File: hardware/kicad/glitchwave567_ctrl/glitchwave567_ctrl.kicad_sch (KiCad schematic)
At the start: 22 parts, among them J1 to MAIN 2x8, SW1 Suntsu SSWFS-S01 (TAP/BYP), SW2 Suntsu SSWFS-S01 (TAP/BYP)

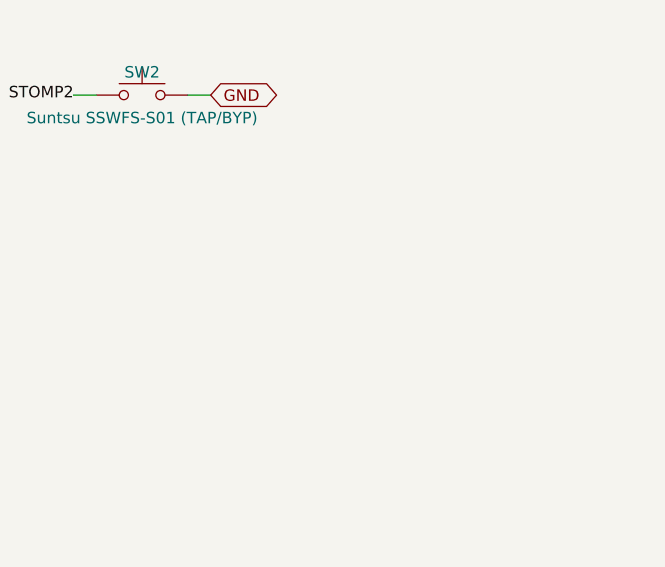
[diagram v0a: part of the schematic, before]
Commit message: hardware: root hierarchy + ERC pass on KiCad 10 (down to lib-mismatch/footprint noise + 2 intentional OTA current-sum waivers)
- root sheet ties all 8 sheets into one project (global-label connectivity, 288 comps / 259 nets stitch verified)
- fixed: U11/U12->U18/U19 ref clash, MCU cap ref clashes, env rectifier D81 feedback returned to virtual ground (was floating FW_IN2), PWR_FLAGs on PICO_VSYS + ctrl rails, off-grid buffer pin
- remaining ERC: footprint_link (assignment pending), lib_symbol_mismatch (v6 embedded vs v10 libs, cosmetic), 2x pin_to_pin Output-Output = LM13700 current summing (by design, noted on sheets)

Co-Authored-By: Claude Fable 5 <noreply@anthropic.com>
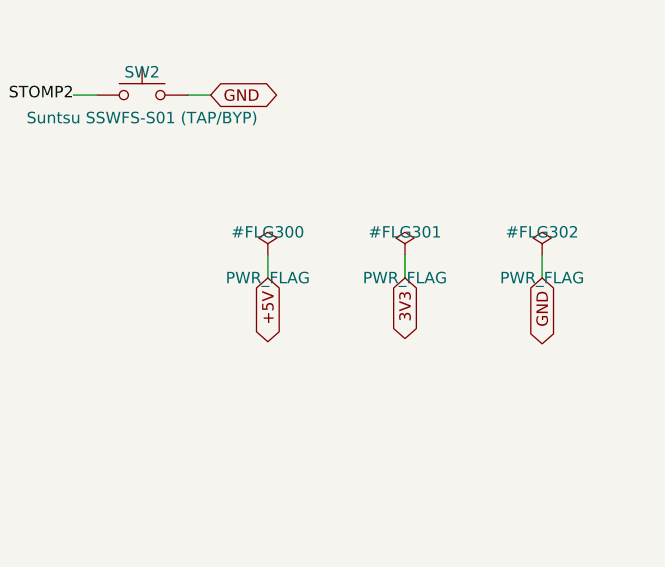
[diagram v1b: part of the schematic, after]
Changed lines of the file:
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@@
+    (stroke (width 0.0))
+  )
+  (wire (pts (xy 280.67 63.5) (xy 280.67 66.04))
+    (stroke (width 0.0))
+  )
+  (wire (pts (xy 295.91 63.5) (xy 295.91 66.04))
+    (stroke (width 0.0))
+  )
+  (wire (pts (xy 311.15 63.5) (xy 311.15 66.04))
     (stroke (width 0.0))
   )
@@
     (effects (font (size 1.27 1.27)))
   )
+  (global_label "+5V" (shape bidirectional) (at 280.67 66.04 270)
+    (effects (font (size 1.27 1.27)))
+  )
+  (global_label "3V3" (shape bidirectional) (at 295.91 66.04 270)
+    (effects (font (size 1.27 1.27)))
+  )
+  (global_label "GND" (shape bidirectional) (at 311.15 66.04 270)
+    (effects (font (size 1.27 1.27)))
+  )
   (symbol (lib_id "Connector_Generic:Conn_02x08_Odd_Even") (at 45.72 63.5 0) (unit 1)
     (in_bom yes) (on_board yes) (dnp no)
@@
         )
       )
+    )
+  )
+  (symbol (lib_id "power:PWR_FLAG") (at 280.67 63.5 0) (unit 1)
+    (in_bom yes) (on_board yes) (dnp no)
+    (property "Reference" "#FLG300" (id 0) (at 280.67 60.96 0)
+      (effects (font (size 1.27 1.27)))
+    )
+    (property "Value" "PWR_FLAG" (id 1) (at 280.67 66.04 0)
+      (effects (font (size 1.27 1.27)))
+    )
+    (property "Footprint" "" (id 2) (at 280.67 63.5 0)
+      (effects (font (size 1.27 1.27)) hide)
+    )
+    (property "Datasheet" "" (id 3) (at 280.67 63.5 0)
+      (effects (font (size 1.27 1.27)) hide)
+    )
+    (instances
+      (project "glitchwave567"
+        (path "/"
+          (reference "#FLG300") (unit 1)
+        )
+      )
+    )
+  )
+  (symbol (lib_id "power:PWR_FLAG") (at 295.91 63.5 0) (unit 1)
+    (in_bom yes) (on_board yes) (dnp no)
+    (property "Reference" "#FLG301" (id 0) (at 295.91 60.96 0)
+      (effects (font (size 1.27 1.27)))
+    )
+    (property "Value" "PWR_FLAG" (id 1) (at 295.91 66.04 0)
+      (effects (font (size 1.27 1.27)))
+    )
+    (property "Footprint" "" (id 2) (at 295.91 63.5 0)
+      (effects (font (size 1.27 1.27)) hide)
+    )
+    (property "Datasheet" "" (id 3) (at 295.91 63.5 0)
+      (effects (font (size 1.27 1.27)) hide)
+    )
+    (instances
+      (project "glitchwave567"
+        (path "/"
+          (reference "#FLG301") (unit 1)
+        )
+      )
+    )
+  )
+  (symbol (lib_id "power:PWR_FLAG") (at 311.15 63.5 0) (unit 1)
+    (in_bom yes) (on_board yes) (dnp no)
+    (property "Reference" "#FLG302" (id 0) (at 311.15 60.96 0)
+      (effects (font (size 1.27 1.27)))
+    )
+    (property "Value" "PWR_FLAG" (id 1) (at 311.15 66.04 0)
+      (effects (font (size 1.27 1.27)))
+    )
+    (property "Footprint" "" (id 2) (at 311.15 63.5 0)
+      (effects (font (size 1.27 1.27)) hide)
+    )
+    (property "Datasheet" "" (id 3) (at 311.15 63.5 0)
+      (effects (font (size 1.27 1.27)) hide)
+    )
+    (instances
+      (project "glitchwave567"
+        (path "/"
+          (reference "#FLG302") (unit 1)
+        )
+      )

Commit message: hardware: footprint phase complete - 297/297 parts footprinted, custom Glitchwave.pretty authored from factory drawings
- Glitchwave.pretty: PJ-603A (pads 7.6/15.1/22.5, slots per HY-WI-32), PJ-3410,
  DC-044A (polarity DMM-verify flagged), ALPS_RK09K1130 (2.5 pitch + 8.8 snap
  legs from ALPS drawing), SSWFS-S01 (slot pads absorb 5.5-6.5 pin-spacing
  ambiguity; NOTE: PC-pin variant thread is 15/32-32 - panel hole D12.2+keyway,
  not M12), RPi_Pico_SMD (official Fig.5 land pattern, row c-c 19.38)
- schgen auto-footprint map wired into add(); all sheets regenerated
- fp-lib-tables for both projects; trims -> Bourns 3224W; clamps -> 1N5819W

Co-Authored-By: Claude Fable 5 <noreply@anthropic.com>
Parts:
- C1, C2, C3, C4, C5, C6: footprint (none) -> Capacitor_SMD:C_0603_1608Metric
- C7: footprint (none) -> Capacitor_SMD:CP_Elec_6.3x7.7
- J1: footprint (none) -> Connector_PinHeader_2.54mm:PinHeader_2x08_P2.54mm_Vertical
- LED1, LED2, LED3, LED4, LED5, LED6: footprint (none) -> LED_SMD:LED_WS2812B_PLCC4_5.0x5.0mm_P3.2mm
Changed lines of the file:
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@@
       (effects (font (size 1.27 1.27)))
     )
-    (property "Footprint" "" (id 2) (at 45.72 63.5 0)
+    (property "Footprint" "Connector_PinHeader_2.54mm:PinHeader_2x08_P2.54mm_Vertical" (id 2) (at 45.72 63.5 0)
       (effects (font (size 1.27 1.27)) hide)
     )
@@
       (effects (font (size 1.27 1.27)))
     )
-    (property "Footprint" "" (id 2) (at 40.64 146.05 0)
+    (property "Footprint" "LED_SMD:LED_WS2812B_PLCC4_5.0x5.0mm_P3.2mm" (id 2) (at 40.64 146.05 0)
       (effects (font (size 1.27 1.27)) hide)
     )
@@
       (effects (font (size 1.27 1.27)))
     )
-    (property "Footprint" "" (id 2) (at 55.88 163.83 0)
+    (property "Footprint" "Capacitor_SMD:C_0603_1608Metric" (id 2) (at 55.88 163.83 0)
       (effects (font (size 1.27 1.27)) hide)
     )
@@
       (effects (font (size 1.27 1.27)))
     )
-    (property "Footprint" "" (id 2) (at 86.36 146.05 0)
+    (property "Footprint" "LED_SMD:LED_WS2812B_PLCC4_5.0x5.0mm_P3.2mm" (id 2) (at 86.36 146.05 0)
       (effects (font (size 1.27 1.27)) hide)
     )
@@
       (effects (font (size 1.27 1.27)))
     )
-    (property "Footprint" "" (id 2) (at 101.6 163.83 0)
+    (property "Footprint" "Capacitor_SMD:C_0603_1608Metric" (id 2) (at 101.6 163.83 0)
       (effects (font (size 1.27 1.27)) hide)
     )
@@
       (effects (font (size 1.27 1.27)))
     )
-    (property "Footprint" "" (id 2) (at 132.07999999999998 146.05 0)
+    (property "Footprint" "LED_SMD:LED_WS2812B_PLCC4_5.0x5.0mm_P3.2mm" (id 2) (at 132.07999999999998 146.05 0)
       (effects (font (size 1.27 1.27)) hide)
     )
@@
       (effects (font (size 1.27 1.27)))
     )
-    (property "Footprint" "" (id 2) (at 147.32 163.83 0)
+    (property "Footprint" "Capacitor_SMD:C_0603_1608Metric" (id 2) (at 147.32 163.83 0)
       (effects (font (size 1.27 1.27)) hide)
     )
@@
       (effects (font (size 1.27 1.27)))
     )
-    (property "Footprint" "" (id 2) (at 177.8 146.05 0)
+    (property "Footprint" "LED_SMD:LED_WS2812B_PLCC4_5.0x5.0mm_P3.2mm" (id 2) (at 177.8 146.05 0)
       (effects (font (size 1.27 1.27)) hide)
     )
@@
       (effects (font (size 1.27 1.27)))
     )
-    (property "Footprint" "" (id 2) (at 193.04000000000002 163.83 0)
+    (property "Footprint" "Capacitor_SMD:C_0603_1608Metric" (id 2) (at 193.04000000000002 163.83 0)
       (effects (font (size 1.27 1.27)) hide)
     )
@@
       (effects (font (size 1.27 1.27)))
     )
-    (property "Footprint" "" (id 2) (at 223.51999999999998 146.05 0)
+    (property "Footprint" "LED_SMD:LED_WS2812B_PLCC4_5.0x5.0mm_P3.2mm" (id 2) (at 223.51999999999998 146.05 0)
       (effects (font (size 1.27 1.27)) hide)
     )
@@
       (effects (font (size 1.27 1.27)))
     )
-    (property "Footprint" "" (id 2) (at 238.76 163.83 0)
+    (property "Footprint" "Capacitor_SMD:C_0603_1608Metric" (id 2) (at 238.76 163.83 0)
       (effects (font (size 1.27 1.27)) hide)
     )
@@
       (effects (font (size 1.27 1.27)))
     )
-    (property "Footprint" "" (id 2) (at 269.24 146.05 0)
+    (property "Footprint" "LED_SMD:LED_WS2812B_PLCC4_5.0x5.0mm_P3.2mm" (id 2) (at 269.24 146.05 0)
       (effects (font (size 1.27 1.27)) hide)
     )
@@
       (effects (font (size 1.27 1.27)))
     )
-    (property "Footprint" "" (id 2) (at 284.48 163.83 0)
+    (property "Footprint" "Capacitor_SMD:C_0603_1608Metric" (id 2) (at 284.48 163.83 0)
       (effects (font (size 1.27 1.27)) hide)
     )
@@
       (effects (font (size 1.27 1.27)))
     )
-    (property "Footprint" "" (id 2) (at 320.04 146.05 0)
-      (effects (font (size 1.27 1.27)) hide)
-    )
+    (property "Footprint" "Capacitor_SMD:CP_Elec_6.3x7.7" (id 2) (at 320.04 146.05 0)
+      (effects (font (size 1.27 1.27)) hide)
+    )

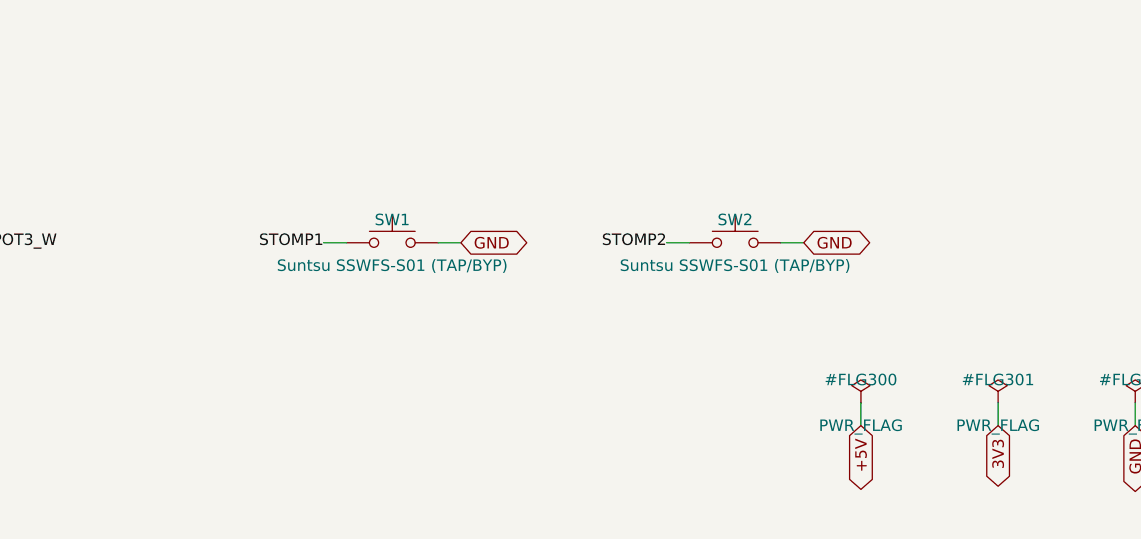
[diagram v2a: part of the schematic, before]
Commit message: Fix CONTROL board stomp switches, regenerate fab release package
Replace the unsourceable Suntsu SSWFS-S01 stomp switch (SW1/SW2) with
Alpha SF12011F-0102-20R-M-011, verified against Alpha's SF12 series
datasheet (2.5mm pitch, Pin1=N.O./Pin2=COM/Pin3=N.C.). Updated the
footprint, schematic Value properties, and PCB routing (re-routed
around the new pad positions after the footprint swap moved absolute
pad locations onto pre-existing trace endpoints). CONTROL board DRC
and ERC are both clean (0 errors).

Also regenerates the full PCBWay fab release package:
- Gerbers for both MAIN and CONTROL boards (re-exported via KiCad)
- Turnkey BOM CSVs with MPNs for both boards (PCBWay format)
- Centroid/placement files for both boards
- BOM.xlsx updated with the new switch part
- README_PCBWAY.md updated to reflect the switch fix and DRC status
- All-in-one release zip with gerbers + BOM + centroid + KiCad source

Co-Authored-By: Claude Sonnet 5 <noreply@anthropic.com>
Claude-Session: https://claude.ai/code/session_012s26yHViqVd1t1x3TF8raS
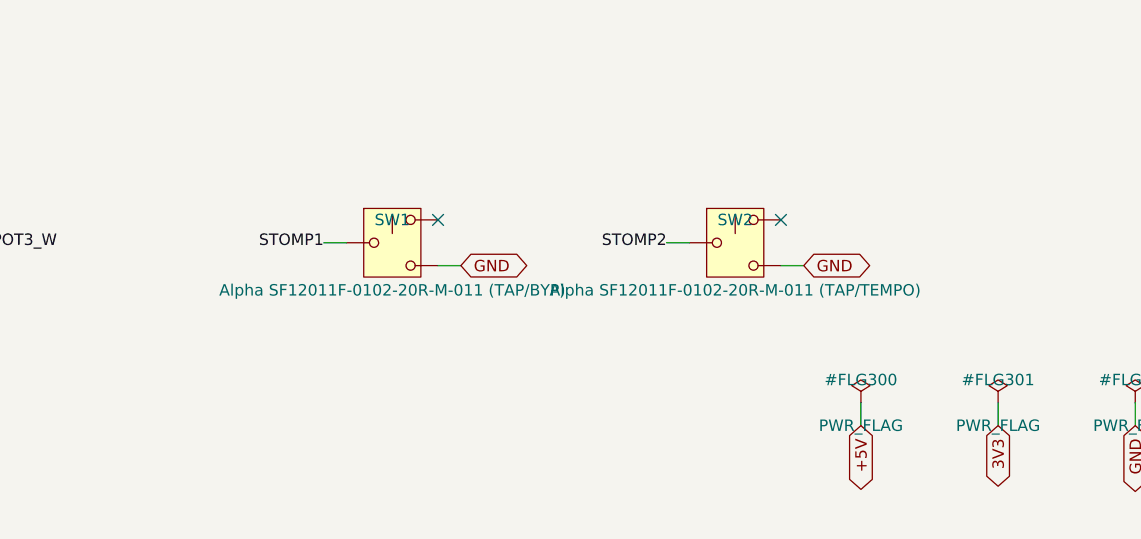
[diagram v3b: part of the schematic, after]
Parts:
- SW1: value Suntsu SSWFS-S01 (TAP/BYP) -> Alpha SF12011F-0102-20R-M-011 (TAP/BYP); footprint Glitchwave:SSWFS-S01 -> Glitchwave:SF12011F-0102-M; symbol Switch:SW_Push -> Switch:SW_Push_SPDT
- SW2: value Suntsu SSWFS-S01 (TAP/BYP) -> Alpha SF12011F-0102-20R-M-011 (TAP/TEMPO); footprint Glitchwave:SSWFS-S01 -> Glitchwave:SF12011F-0102-M; symbol Switch:SW_Push -> Switch:SW_Push_SPDT
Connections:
- net GND: now also SW1.3 (C), SW2.3 (C); no longer SW1.2, SW2.2
- net STOMP1: now also SW1.2 (B); no longer SW1.1
- net STOMP2: now also SW2.2 (B); no longer SW2.1
- no-connect marks 2 -> 4
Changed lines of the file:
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@@
   )
   (no_connect (at 40.64 73.66))
+  (no_connect (at 233.68 43.18))
+  (no_connect (at 271.78 43.18))
   (no_connect (at 276.86 146.05))
   (wire (pts (xy 40.64 55.88) (xy 38.1 55.88))
@@
     (stroke (width 0.0))
   )
-  (wire (pts (xy 233.68 45.72) (xy 236.22 45.72))
+  (wire (pts (xy 233.68 48.26) (xy 236.22 48.26))
     (stroke (width 0.0))
   )
@@
     (stroke (width 0.0))
   )
-  (wire (pts (xy 271.78 45.72) (xy 274.32 45.72))
+  (wire (pts (xy 271.78 48.26) (xy 274.32 48.26))
     (stroke (width 0.0))
   )
@@
     (effects (font (size 1.27 1.27)))
   )
-  (global_label "GND" (shape bidirectional) (at 236.22 45.72 0)
-    (effects (font (size 1.27 1.27)))
-  )
-  (global_label "GND" (shape bidirectional) (at 274.32 45.72 0)
+  (global_label "GND" (shape bidirectional) (at 236.22 48.26 0)
+    (effects (font (size 1.27 1.27)))
+  )
+  (global_label "GND" (shape bidirectional) (at 274.32 48.26 0)
     (effects (font (size 1.27 1.27)))
   )
@@
     )
   )
-  (symbol (lib_id "Switch:SW_Push") (at 228.6 45.72 0) (unit 1)
+  (symbol (lib_id "Switch:SW_Push_SPDT") (at 228.6 45.72 0) (unit 1)
     (in_bom yes) (on_board yes) (dnp no)
     (property "Reference" "SW1" (id 0) (at 228.6 43.18 0)
       (effects (font (size 1.27 1.27)))
     )
-    (property "Value" "Suntsu SSWFS-S01 (TAP/BYP)" (id 1) (at 228.6 48.26 0)
-      (effects (font (size 1.27 1.27)))
-    )
-    (property "Footprint" "Glitchwave:SSWFS-S01" (id 2) (at 228.6 45.72 0)
-      (effects (font (size 1.27 1.27)) hide)
-    )
-    (property "Datasheet" "" (id 3) (at 228.6 45.72 0)
+    (property "Value" "Alpha SF12011F-0102-20R-M-011 (TAP/BYP)" (id 1) (at 228.6 51.0 0)
+      (effects (font (size 1.27 1.27)))
+    )
+    (property "Footprint" "Glitchwave:SF12011F-0102-M" (id 2) (at 228.6 45.72 0)
+      (effects (font (size 1.27 1.27)) hide)
+    )
+    (property "Datasheet" "https://www.mouser.com/datasheet/2/13/Foot_Switch___SF12_Series-2303797.pdf" (id 3) (at 228.6 45.72 0)
       (effects (font (size 1.27 1.27)) hide)
     )
@@
     )
   )
-  (symbol (lib_id "Switch:SW_Push") (at 266.7 45.72 0) (unit 1)
+  (symbol (lib_id "Switch:SW_Push_SPDT") (at 266.7 45.72 0) (unit 1)
     (in_bom yes) (on_board yes) (dnp no)
     (property "Reference" "SW2" (id 0) (at 266.7 43.18 0)
       (effects (font (size 1.27 1.27)))
     )
-    (property "Value" "Suntsu SSWFS-S01 (TAP/BYP)" (id 1) (at 266.7 48.26 0)
-      (effects (font (size 1.27 1.27)))
-    )
-    (property "Footprint" "Glitchwave:SSWFS-S01" (id 2) (at 266.7 45.72 0)
-      (effects (font (size 1.27 1.27)) hide)
-    )
-    (property "Datasheet" "" (id 3) (at 266.7 45.72 0)
-      (effects (font (size 1.27 1.27)) hide)
-    )
+    (property "Value" "Alpha SF12011F-0102-20R-M-011 (TAP/TEMPO)" (id 1) (at 266.7 51.0 0)
+      (effects (font (size 1.27 1.27)))
+    )
+    (property "Footprint" "Glitchwave:SF12011F-0102-M" (id 2) (at 266.7 45.72 0)
+      (effects (font (size 1.27 1.27)) hide)
+    )
+    (property "Datasheet" "https://www.mouser.com/datasheet/2/13/Foot_Switch___SF12_Series-2303797.pdf" (id 3) (at 266.7 45.72 0)
+      (effects (font (size 1.27 1.27)) hide)
+    )

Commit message: Rev 8: third stomp (SW3) + STOMP3 to GP22, boards/BOM/fab package updated
CONTROL: SW3 at (69,96); SW1/SW2 outboard to 23.28/114.72 (1.800in pitch);
LED4/LED5 follow; C7 +1.5mm east; 3 GND stitch vias cleared from new pad rows;
/POT3_W detoured around SW2's new COM pad; stomp silk now A/B/C; STOMP3 on
spare J1 pin 15. Fixes schematic pin1/pin3 inversion on SW1/SW2 (GND belongs
on N.O.; PCB was already right). DRC 0 errors.

MAIN: R175 10k pullup + C125 100n added; STOMP3 routed J10.15 -> GP22 (Pico
pad 29). DRC/ERC at pre-existing baselines. BOM.xlsx updated (SW qty 3, R/C
qty bumps, stale Suntsu README lines replaced). Fab package regenerated both
boards: Glitchwave567_PCBWay_Release_20260921.zip, README_PCBWAY rev 0.6.

Enclosure drill template still stale: needs three D12.2 at centreline +/-45.72mm.

Co-Authored-By: Claude Fable 5 <noreply@anthropic.com>
Claude-Session: https://claude.ai/code/session_01ArRoxLtCyE7DZoHE3DcYLs
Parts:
- added SW3: Alpha SF12011F-0102-20R-M-011 (STOMP3), Glitchwave:SF12011F-0102-M, symbol Switch:SW_Push_SPDT
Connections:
- net GND: now also SW1.1 (A), SW2.1 (A), SW3.1 (A); no longer SW1.3 (C), SW2.3 (C)
- net STOMP3: now reaches J1.15 (Pin_15)
- net STOMP3: now also SW3.2 (B)
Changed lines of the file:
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@@
     (company "Illicit Apothecary")
   )
-  (no_connect (at 40.64 73.66))
-  (no_connect (at 233.68 43.18))
-  (no_connect (at 271.78 43.18))
+  (wire (pts (xy 40.64 73.66) (xy 38.1 73.66))
+    (stroke (width 0.0))
+  )
+  (label "STOMP3" (at 38.1 73.66 180)
+    (effects (font (size 1.27 1.27)))
+  )
+  (no_connect (at 233.68 48.26))
+  (no_connect (at 271.78 48.26))
   (no_connect (at 276.86 146.05))
   (wire (pts (xy 40.64 55.88) (xy 38.1 55.88))
@@
     (stroke (width 0.0))
   )
-  (wire (pts (xy 233.68 48.26) (xy 236.22 48.26))
+  (wire (pts (xy 233.68 43.18) (xy 236.22 43.18))
     (stroke (width 0.0))
   )
@@
     (stroke (width 0.0))
   )
-  (wire (pts (xy 271.78 48.26) (xy 274.32 48.26))
+  (wire (pts (xy 271.78 43.18) (xy 274.32 43.18))
     (stroke (width 0.0))
   )
@@
     (effects (font (size 1.27 1.27)))
   )
-  (global_label "GND" (shape bidirectional) (at 236.22 48.26 0)
-    (effects (font (size 1.27 1.27)))
-  )
-  (global_label "GND" (shape bidirectional) (at 274.32 48.26 0)
+  (global_label "GND" (shape bidirectional) (at 236.22 43.18 0)
+    (effects (font (size 1.27 1.27)))
+  )
+  (global_label "GND" (shape bidirectional) (at 274.32 43.18 0)
     (effects (font (size 1.27 1.27)))
   )
@@
     )
   )
+  (symbol (lib_id "Switch:SW_Push_SPDT") (at 304.8 45.72 0) (unit 1)
+    (in_bom yes) (on_board yes) (dnp no)
+    (property "Reference" "SW3" (id 0) (at 304.8 43.18 0)
+      (effects (font (size 1.27 1.27)))
+    )
+    (property "Value" "Alpha SF12011F-0102-20R-M-011 (STOMP3)" (id 1) (at 304.8 51.0 0)
+      (effects (font (size 1.27 1.27)))
+    )
+    (property "Footprint" "Glitchwave:SF12011F-0102-M" (id 2) (at 304.8 45.72 0)
+      (effects (font (size 1.27 1.27)) hide)
+    )
+    (property "Datasheet" "https://www.mouser.com/datasheet/2/13/Foot_Switch___SF12_Series-2303797.pdf" (id 3) (at 304.8 45.72 0)
+      (effects (font (size 1.27 1.27)) hide)
+    )
+    (instances
+      (project "glitchwave567"
+        (path "/"
+          (reference "SW3") (unit 1)
+        )
+      )
+    )
+  )
+  (wire (pts (xy 299.72 45.72) (xy 297.18 45.72))
+    (stroke (width 0.0))
+  )
+  (label "STOMP3" (at 297.18 45.72 180)
+    (effects (font (size 1.27 1.27)))
+  )
+  (wire (pts (xy 309.88 43.18) (xy 312.42 43.18))
+    (stroke (width 0.0))
+  )
+  (global_label "GND" (shape bidirectional) (at 312.42 43.18 0)
+    (effects (font (size 1.27 1.27)))
+  )
+  (no_connect (at 309.88 48.26))
   (symbol (lib_id "LED:WS2812B") (at 40.64 146.05 0) (unit 1)
     (in_bom yes) (on_board yes) (dnp no)
